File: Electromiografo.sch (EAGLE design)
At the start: 41 parts, among them IC1 ESP32-S3-WROOM-1-N16R8, IC10 LMV321IDBVRG4, IC2 MCP73831T-2DCI_OT, IC3 741G3157DBVR, IC4 LP38692MP-3.3_NOPB, IC5 REF2033AIDDCT, IC6 LMV321IDBVRG4, IC7 LMV321IDBVRG4, IC8 LMV321IDBVRG4, IC9 AD8223ARMZ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

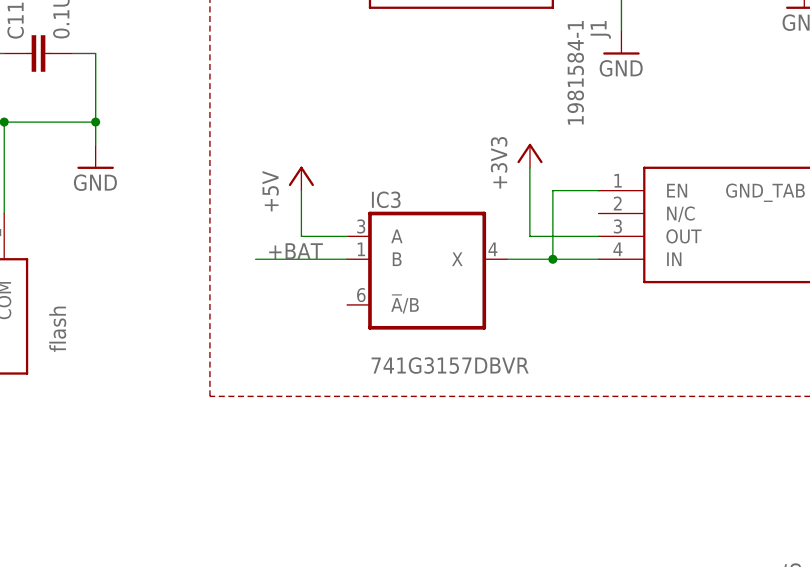
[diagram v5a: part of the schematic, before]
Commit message: corregido el switche
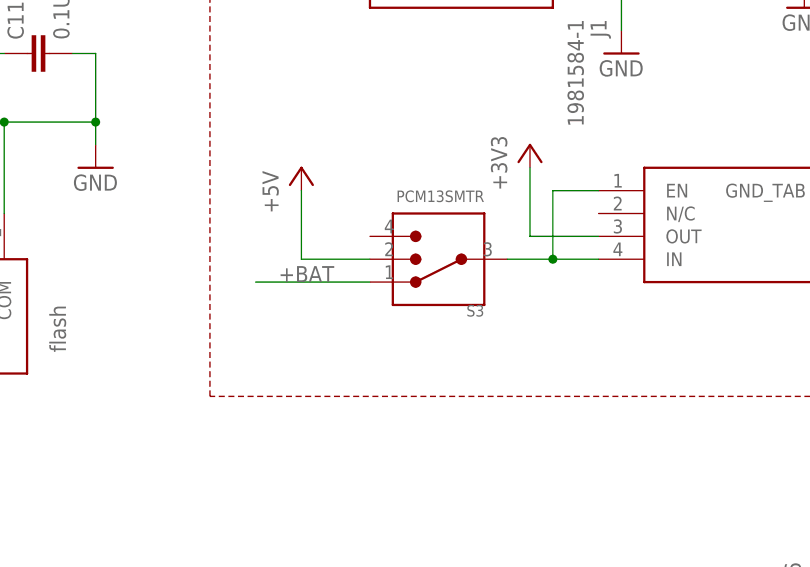
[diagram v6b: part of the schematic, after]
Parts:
- removed IC3: 741G3157DBVR, 74xx-little-us:741G3157DBVR
- added S3: PCM13SMTR, PCM13SMTR:PCM13SMTR
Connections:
- net +5V: now also S3.2; no longer IC3G$1.A
- net +BAT: now also S3.1; no longer IC3G$1.B
- net N$26: now also S3.3; no longer IC3G$1.X
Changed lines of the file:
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@@
 <part name="GND10" library="supply1" library_urn="urn:adsk.eagle:library:371" deviceset="GND" device=""/>
 <part name="P+2" library="supply1" library_urn="urn:adsk.eagle:library:371" deviceset="+5V" device=""/>
-<part name="IC3" library="74xx-little-us" library_urn="urn:adsk.eagle:library:87" deviceset="74*1G3157" device="DBVR" package3d_urn="urn:adsk.eagle:package:2414/3"/>
 <part name="IC4" library="SamacSys_Parts" deviceset="LP38692MP-3.3_NOPB" device=""/>
 <part name="+3V5" library="supply1" library_urn="urn:adsk.eagle:library:371" deviceset="+3V3" device=""/>
@@
 <part name="S1" library="SamacSys_Parts" deviceset="B3U-1000PM" device=""/>
 <part name="S2" library="SamacSys_Parts" deviceset="B3U-1000PM" device=""/>
+<part name="S3" library="PCM13SMTR" deviceset="PCM13SMTR" device=""/>
 </parts>
 <sheets>
@@
 <attribute name="VALUE" x="294.64" y="213.36" size="1.778" layer="96" rot="R90"/>
 </instance>
-<instance part="IC3" gate="G$1" x="243.84" y="154.94" smashed="yes">
-<attribute name="NAME" x="238.76" y="163.195" size="1.778" layer="95"/>
-<attribute name="VALUE" x="238.76" y="144.78" size="1.778" layer="96"/>
-</instance>
 <instance part="IC4" gate="G$1" x="264.16" y="165.1" smashed="yes">
 <attribute name="NAME" x="290.83" y="172.72" size="1.778" layer="95" align="center-left"/>
@@
 <attribute name="NAME" x="78.74" y="140.97" size="1.778" layer="95" rot="MR270" align="center-left"/>
 <attribute name="VALUE" x="81.28" y="140.97" size="1.778" layer="96" rot="MR270" align="center-left"/>
+</instance>
+<instance part="S3" gate="G$1" x="246.38" y="157.48" smashed="yes" rot="R180">
+<attribute name="NAME" x="251.46978125" y="152.39021875" size="1.27245" layer="95" rot="R180"/>
+<attribute name="VALUE" x="251.46605" y="165.10906875" size="1.271509375" layer="96" rot="R180"/>
 </instance>
 </instances>
@@
 </segment>
 <segment>
-<pinref part="IC3" gate="G$1" pin="A"/>
 <pinref part="P+3" gate="1" pin="+5V"/>
-<wire x1="236.22" y1="160.02" x2="231.14" y2="160.02" width="0.1524" layer="91"/>
-<wire x1="231.14" y1="160.02" x2="231.14" y2="165.1" width="0.1524" layer="91"/>
+<wire x1="231.14" y1="157.48" x2="231.14" y2="165.1" width="0.1524" layer="91"/>
+<pinref part="S3" gate="G$1" pin="2"/>
+<wire x1="231.14" y1="157.48" x2="238.76" y2="157.48" width="0.1524" layer="91"/>
 </segment>
 </net>
@@
 <net name="N$26" class="0">
 <segment>
-<pinref part="IC3" gate="G$1" pin="X"/>
 <pinref part="IC4" gate="G$1" pin="IN"/>
 <wire x1="254" y1="157.48" x2="259.08" y2="157.48" width="0.1524" layer="91"/>
@@
 <wire x1="259.08" y1="165.1" x2="259.08" y2="157.48" width="0.1524" layer="91"/>
 <junction x="259.08" y="157.48"/>
+<pinref part="S3" gate="G$1" pin="3"/>
 </segment>
 </net>
 <net name="+BAT" class="0">
-<segment>
-<pinref part="IC3" gate="G$1" pin="B"/>
-<wire x1="236.22" y1="157.48" x2="226.06" y2="157.48" width="0.1524" layer="91"/>
-<label x="227.33" y="157.48" size="1.778" layer="95"/>
-</segment>
 <segment>
 <pinref part="IC2" gate="G$1" pin="VBAT"/>
@@
 <label x="556.26" y="-127" size="1.778" layer="95" rot="R270"/>
 </segment>
-</net>
+<segment>
+<wire x1="238.76" y1="154.94" x2="226.06" y2="154.94" width="0.1524" layer="91"/>
+<pinref part="S3" gate="G$1" pin="1"/>
+<label x="228.6" y="154.94" size="1.778" layer="95"/>
+</segment>
+</net>

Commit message: Modificaciones esquematico, version 2 de pcb
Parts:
- removed LED1: (no value), PulseOximeterECG_AU:LEDCHIP-LED0805
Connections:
- net N$12 renamed RX
- net N$15 renamed TX
- net N$2 renamed RESET
- net N$4 renamed DAC1
- net N$6 renamed DAC2
- net N$7 renamed TOUCHPAD1
- net N$8 renamed TOUCHPAD2
- net N$9 renamed TOUCHPAD3
- removed net N$10: IC1.IO21
- removed net N$11: IC1.IO47
- removed net N$14: LED1.C, R3.2
- removed net N$16: IC1.IO2
- removed net N$21: JP1.2
- removed net N$22: JP1.1
- new net SCL: IC1.IO2, JP1.1
- net +5V: now also R3.2; no longer LED1.A
- net D+: now also IC1.IO12
- net D-: now also IC1.IO11
- net SDA: now also JP1.2
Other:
- note removed: "DAC1"
- note removed: "DAC2"
- note removed: "LED1"
- note removed: "LED2"
- note removed: "RESET32"
- note removed: "RX"
- note removed: "SCL"
- note removed: "SDA"
- note removed: "TOUCHPAD1"
- note removed: "TOUCHPAD2"
- note removed: "TOUCHPAD3"
- note removed: "TX"
- moved on the sheet: C1, C2, R1, R2, R3

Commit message: Se realozaron ajustes finales a la pcb
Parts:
- renumbered IC1 to ESP32, IC4 to REG, IC9 to INA, J1 to USB, J2 to CBAT, S3 to S3-1
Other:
- moved on the sheet: C1, C2, R2
